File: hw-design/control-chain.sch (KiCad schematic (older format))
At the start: 37 parts, among them J1 RJ45_CHAIN_MAIN, J2 RJ45_CHAIN_EXTENSION, Q1 MMBT3904, Q2 MMBT3906, Q4 MMBT3904, Q5 MMBT3904, Q6 MMBT3904, U4 MAX13450E

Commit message: changing control chain schematic to use default kicad components library
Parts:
- removed J1: RJ45_CHAIN_MAIN, MOD_Footprints_Lib:RJ45-RJHSE5084, symbol RJ45_CHAIN
- removed J2: RJ45_CHAIN_EXTENSION, MOD_Footprints_Lib:RJ45-RJHSE5084, symbol RJ45_CHAIN
- added J? (x2): RJ45_LEDS, symbol RJ45_LEDS
- C18, C20, C6: value 100nF_X7R -> 100nF X7R
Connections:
- net labels added: +3.3VP, GNDD, VDD
- net labels removed: +3.3V, DGND, VCC
- wire segments 133 -> 161
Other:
- moved on the sheet: C19, C20, C5, C6, Q1, Q4, R1, R2, R3, R4, R44, R48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

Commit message: ERC passing
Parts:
- gave numbers to parts that had none: 2
- renumbered C6 to C10, C20 to C11, C18 to C7, C5 to C8, C19 to C9, Q6 to Q1, Q1 to Q2, Q4 to Q3, Q5 to Q4, Q2 to Q5, R54 to R1, R44 to R11, R48 to R12, R31 to R13, R9 to R14, R49 to R15, R52 to R16, R50 to R17, R51 to R18, R12 to R19, R1 to R2, R13 to R20, R53 to R21, R14 to R22, R5 to R3, R6 to R5, R3 to R6, R2 to R8, R8 to R9, U4 to U3
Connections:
- wire segments 161 -> 132

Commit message: wip: footprint association using default kicad libraries
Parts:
- C10, C11, C7: footprint MOD_Footprints_Lib:SM0603 -> Capacitors_SMD:C_0603
- C8, C9: footprint MOD_Footprints_Lib:CAP_RAD_5MM -> Capacitors_ThroughHole:Capacitor5x6RM2.5
- D2, D3: footprint MOD_Footprints_Lib:SOD123 -> Diodes_SMD:SOD-123
- J1, J2: footprint (none) -> MOD_Footprints:RJ45-RJHSE5084
- Q1, Q2, Q3, Q4: footprint (none) -> Transistors_SMD:sot23
- Q5: footprint MOD_Footprints_Lib:SOT23 -> Transistors_SMD:sot23
- R1, R10, R12, R13, R14, R15, R16, R17, R18, R19, R2, R20, R21, R22, R7: footprint MOD_Footprints_Lib:SM0603 -> Resistors_SMD:R_0603
- R11, R3, R4, R5, R6: footprint MOD_Footprints_Lib:SM0805 -> Resistors_SMD:R_0603
- R8, R9: footprint MOD_Footprints_Lib:SM1210 -> Resistors_SMD:R_1210
- U3: footprint TSSOP-14EP -> Housings_SSOP:TSSOP-14_4.4x5mm_Pitch0.65mm
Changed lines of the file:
@@
 F 0 "R5" V 2500 850 40  0000 C CNN
 F 1 "1K2" V 2557 1051 40  0000 C CNN
-F 2 "MOD_Footprints_Lib:SM0805" V 2480 1050 30  0001 C CNN
+F 2 "Resistors_SMD:R_0603" V 2480 1050 30  0001 C CNN
 F 3 "~" H 2550 1050 30  0000 C CNN
 	1    2550 1050
@@
 F 0 "R3" V 2450 1250 40  0000 C CNN
 F 1 "1K2" V 2407 1051 40  0000 C CNN
-F 2 "MOD_Footprints_Lib:SM0805" V 2330 1050 30  0001 C CNN
+F 2 "Resistors_SMD:R_0603" V 2330 1050 30  0001 C CNN
 F 3 "~" H 2400 1050 30  0000 C CNN
 	1    2400 1050
@@
 F 0 "R6" V 2600 4550 40  0000 C CNN
 F 1 "1K2" V 2557 4351 40  0000 C CNN
-F 2 "MOD_Footprints_Lib:SM0805" V 2480 4350 30  0001 C CNN
+F 2 "Resistors_SMD:R_0603" V 2480 4350 30  0001 C CNN
 F 3 "~" H 2550 4350 30  0000 C CNN
 	1    2550 4350
@@
 F 0 "R2" V 1500 2450 40  0000 C CNN
 F 1 "10k" V 1607 2451 40  0000 C CNN
-F 2 "MOD_Footprints_Lib:SM0603" V 1530 2450 30  0001 C CNN
+F 2 "Resistors_SMD:R_0603" V 1530 2450 30  0001 C CNN
 F 3 "~" H 1600 2450 30  0000 C CNN
 	1    1600 2450
@@
 F 0 "R13" V 5050 7050 40  0000 C CNN
 F 1 "10k" V 5007 6801 40  0000 C CNN
-F 2 "MOD_Footprints_Lib:SM0603" V 4930 6800 30  0001 C CNN
+F 2 "Resistors_SMD:R_0603" V 4930 6800 30  0001 C CNN
 F 3 "~" H 5000 6800 30  0000 C CNN
 	1    5000 6800
@@
 F 0 "R7" V 3650 5550 40  0000 C CNN
 F 1 "10k" V 3557 5551 40  0000 C CNN
-F 2 "MOD_Footprints_Lib:SM0603" V 3480 5550 30  0001 C CNN
+F 2 "Resistors_SMD:R_0603" V 3480 5550 30  0001 C CNN
 F 3 "~" H 3550 5550 30  0000 C CNN
 	1    3550 5550
@@
 F 0 "D3" H 1798 6112 40  0000 C CNN
 F 1 "MMSZ5242B" H 1796 5978 30  0000 C CNN
-F 2 "MOD_Footprints_Lib:SOD123" H 1800 6050 60  0001 C CNN
+F 2 "Diodes_SMD:SOD-123" H 1800 6050 60  0001 C CNN
 F 3 "" H 1800 6050 60  0000 C CNN
 	1    1800 6050
@@
 F 0 "D2" H 1598 6112 40  0000 C CNN
 F 1 "MMSZ5242B" H 1598 5984 30  0000 C CNN
-F 2 "MOD_Footprints_Lib:SOD123" H 1600 6050 60  0001 C CNN
+F 2 "Diodes_SMD:SOD-123" H 1600 6050 60  0001 C CNN
 F 3 "" H 1600 6050 60  0000 C CNN
 	1    1600 6050
@@
 F 0 "C7" V 2050 7075 40  0000 L CNN
 F 1 "100nF X7R" V 2125 7075 40  0000 L CNN
-F 2 "MOD_Footprints_Lib:SM0603" H 2038 7100 30  0001 C CNN
+F 2 "Capacitors_SMD:C_0603" H 2038 7100 30  0001 C CNN
 F 3 "~" H 2000 7250 60  0000 C CNN
 	1    2000 7250
@@
 F 0 "R10" V 3900 5550 40  0000 C CNN
 F 1 "10k" V 3807 5551 40  0000 C CNN
-F 2 "MOD_Footprints_Lib:SM0603" V 3730 5550 30  0001 C CNN
+F 2 "Resistors_SMD:R_0603" V 3730 5550 30  0001 C CNN
 F 3 "~" H 3800 5550 30  0000 C CNN
 	1    3800 5550
@@
 F 0 "R11" V 4400 6150 40  0000 C CNN
 F 1 "0R/NC" V 4307 6151 40  0000 C CNN
-F 2 "MOD_Footprints_Lib:SM0805" V 4230 6150 30  0001 C CNN
+F 2 "Resistors_SMD:R_0603" V 4230 6150 30  0001 C CNN
 F 3 "~" H 4300 6150 30  0000 C CNN
 	1    4300 6150
@@
 F 0 "R9" V 3850 4600 40  0000 C CNN
 F 1 "100R 0.5W" V 3700 4350 40  0000 C CNN
-F 2 "MOD_Footprints_Lib:SM1210" V 3730 4350 30  0001 C CNN
+F 2 "Resistors_SMD:R_1210" V 3730 4350 30  0001 C CNN
 F 3 "~" H 3800 4350 30  0000 C CNN
 	1    3800 4350
@@
 F 0 "R8" V 3850 2800 40  0000 C CNN
 F 1 "100R 0.5W" V 3700 2550 40  0000 C CNN
-F 2 "MOD_Footprints_Lib:SM1210" V 3730 2550 30  0001 C CNN
+F 2 "Resistors_SMD:R_1210" V 3730 2550 30  0001 C CNN
 F 3 "~" H 3800 2550 30  0000 C CNN
 	1    3800 2550
@@
 F 0 "C8" V 4550 4350 50  0000 L CNN
 F 1 "100uF" V 4300 4150 50  0000 L CNN
-F 2 "MOD_Footprints_Lib:CAP_RAD_5MM" H 4450 4250 60  0001 C CNN
+F 2 "Capacitors_ThroughHole:Capacitor5x6RM2.5" H 4450 4250 60  0001 C CNN
 F 3 "~" H 4450 4250 60  0000 C CNN
 	1    4450 4250
@@
 F 0 "C10" V 4750 4350 40  0000 L CNN
 F 1 "100nF X7R" V 4950 4100 40  0000 L CNN
-F 2 "MOD_Footprints_Lib:SM0603" H 4838 4100 30  0001 C CNN
+F 2 "Capacitors_SMD:C_0603" H 4838 4100 30  0001 C CNN
 F 3 "~" H 4800 4250 60  0000 C CNN
 	1    4800 4250
@@
 F 0 "R20" V 7350 3000 40  0000 C CNN
 F 1 "10k" V 7457 3001 40  0000 C CNN
-F 2 "MOD_Footprints_Lib:SM0603" V 7380 3000 30  0001 C CNN
+F 2 "Resistors_SMD:R_0603" V 7380 3000 30  0001 C CNN
 F 3 "~" H 7450 3000 30  0000 C CNN
 	1    7450 3000
@@
 F 0 "R19" V 6950 3350 40  0000 C CNN
 F 1 "100k" V 7057 3351 40  0000 C CNN
-F 2 "MOD_Footprints_Lib:SM0603" V 6980 3350 30  0001 C CNN
+F 2 "Resistors_SMD:R_0603" V 6980 3350 30  0001 C CNN
 F 3 "~" H 7050 3350 30  0000 C CNN
 	1    7050 3350
@@
 F 0 "R22" V 8400 4000 40  0000 C CNN
 F 1 "10k" V 8507 4001 40  0000 C CNN
-F 2 "MOD_Footprints_Lib:SM0603" V 8430 4000 30  0001 C CNN
+F 2 "Resistors_SMD:R_0603" V 8430 4000 30  0001 C CNN
 F 3 "~" H 8500 4000 30  0000 C CNN
 	1    8500 4000
@@
 F 0 "Q5" H 8400 3200 50  0000 R CNN
 F 1 "MMBT3906" H 8400 3500 50  0000 R CNN
-F 2 "MOD_Footprints_Lib:SOT23" H 8400 3350 60  0001 C CNN
+F 2 "Transistors_SMD:sot23" H 8400 3350 60  0001 C CNN
 F 3 "" H 8400 3350 60  0000 C CNN
 	1    8400 3350
@@
 F 0 "R12" V 4850 3750 40  0000 C CNN
 F 1 "100k" V 4807 3501 40  0000 C CNN
-F 2 "MOD_Footprints_Lib:SM0603" V 4730 3500 30  0001 C CNN
+F 2 "Resistors_SMD:R_0603" V 4730 3500 30  0001 C CNN
 F 3 "~" H 4800 3500 30  0000 C CNN
 	1    4800 3500
@@
 F 0 "C9" V 4900 2400 50  0000 L CNN
 F 1 "100uF" V 4650 2200 50  0000 L CNN
-F 2 "MOD_Footprints_Lib:CAP_RAD_5MM" H 4800 2300 60  0001 C CNN
+F 2 "Capacitors_ThroughHole:Capacitor5x6RM2.5" H 4800 2300 60  0001 C CNN
 F 3 "~" H 4800 2300 60  0000 C CNN
 	1    4800 2300
@@
 F 0 "C11" V 5100 2400 40  0000 L CNN
 F 1 "100nF X7R" V 5300 2150 40  0000 L CNN
-F 2 "MOD_Footprints_Lib:SM0603" H 5188 2150 30  0001 C CNN
+F 2 "Capacitors_SMD:C_0603" H 5188 2150 30  0001 C CNN
 F 3 "~" H 5150 2300 60  0000 C CNN
 	1    5150 2300
@@
 F 0 "R16" V 5550 2550 40  0000 C CNN
 F 1 "100k" V 5507 2301 40  0000 C CNN
-F 2 "MOD_Footprints_Lib:SM0603" V 5430 2300 30  0001 C CNN
+F 2 "Resistors_SMD:R_0603" V 5430 2300 30  0001 C CNN
 F 3 "~" H 5500 2300 30  0000 C CNN
 	1    5500 2300
@@
 F 0 "R18" V 5900 6350 40  0000 C CNN
 F 1 "10k" V 5857 6101 40  0000 C CNN
-F 2 "MOD_Footprints_Lib:SM0603" V 5780 6100 30  0001 C CNN
+F 2 "Resistors_SMD:R_0603" V 5780 6100 30  0001 C CNN
 F 3 "~" H 5850 6100 30  0000 C CNN
 	1    5850 6100
@@
 F 0 "R17" V 5900 5400 40  0000 C CNN
 F 1 "10k" V 5857 5151 40  0000 C CNN
-F 2 "MOD_Footprints_Lib:SM0603" V 5780 5150 30  0001 C CNN
+F 2 "Resistors_SMD:R_0603" V 5780 5150 30  0001 C CNN
 F 3 "~" H 5850 5150 30  0000 C CNN
 	1    5850 5150
@@
 F 0 "R14" V 5350 5500 40  0000 C CNN
 F 1 "100k" V 5457 5501 40  0000 C CNN
-F 2 "MOD_Footprints_Lib:SM0603" V 5380 5500 30  0001 C CNN
+F 2 "Resistors_SMD:R_0603" V 5380 5500 30  0001 C CNN
 F 3 "~" H 5450 5500 30  0000 C CNN
 	1    5450 5500
@@
 F 0 "R15" V 5350 6450 40  0000 C CNN
 F 1 "100k" V 5457 6451 40  0000 C CNN
-F 2 "MOD_Footprints_Lib:SM0603" V 5380 6450 30  0001 C CNN
+F 2 "Resistors_SMD:R_0603" V 5380 6450 30  0001 C CNN
 F 3 "~" H 5450 6450 30  0000 C CNN
 	1    5450 6450
@@
 F 0 "R21" V 7750 3350 40  0000 C CNN
 F 1 "1k" V 7857 3351 40  0000 C CNN
-F 2 "MOD_Footprints_Lib:SM0603" V 7780 3350 30  0001 C CNN
+F 2 "Resistors_SMD:R_0603" V 7780 3350 30  0001 C CNN
 F 3 "~" H 7850 3350 30  0000 C CNN
 	1    7850 3350
@@
 F 0 "R4" V 2450 4550 40  0000 C CNN
 F 1 "1K2" V 2407 4351 40  0000 C CNN
-F 2 "MOD_Footprints_Lib:SM0805" V 2330 4350 30  0001 C CNN
+F 2 "Resistors_SMD:R_0603" V 2330 4350 30  0001 C CNN
 F 3 "~" H 2400 4350 30  0000 C CNN
 	1    2400 4350
@@
 F 0 "R1" V 1450 3400 40  0000 C CNN
 F 1 "10k" V 1557 3401 40  0000 C CNN
-F 2 "MOD_Footprints_Lib:SM0603" V 1480 3400 30  0001 C CNN
+F 2 "Resistors_SMD:R_0603" V 1480 3400 30  0001 C CNN
 F 3 "~" H 1550 3400 30  0000 C CNN
 	1    1550 3400
@@
 F 0 "U3" H 2700 7100 60  0000 C CNN
 F 1 "MAX13450E" H 2950 5600 60  0000 C CNN
-F 2 "TSSOP-14EP" H 2600 6950 40  0001 C CNN
+F 2 "Housings_SSOP:TSSOP-14_4.4x5mm_Pitch0.65mm" H 2600 6950 40  0001 C CNN
 F 3 "" H 2725 6250 60  0000 C CNN
 	1    2700 6350
@@
 F 0 "Q3" H 5100 5000 50  0000 R CNN
 F 1 "MMBT3904" H 5100 5300 50  0000 R CNN
-F 2 "" H 5100 5150 60  0000 C CNN
+F 2 "Transistors_SMD:sot23" H 5100 5150 60  0001 C CNN
 F 3 "" H 5100 5150 60  0000 C CNN
 	1    5100 5150
@@
 F 0 "Q4" H 5100 5950 50  0000 R CNN
 F 1 "MMBT3904" H 5350 6350 50  0000 R CNN
-F 2 "" H 5100 6100 60  0000 C CNN
+F 2 "Transistors_SMD:sot23" H 5100 6100 60  0001 C CNN
 F 3 "" H 5100 6100 60  0000 C CNN
 	1    5100 6100
@@
 F 0 "Q2" H 2300 2300 50  0000 R CNN
 F 1 "MMBT3904" H 2300 2600 50  0000 R CNN
-F 2 "" H 2300 2450 60  0000 C CNN
+F 2 "Transistors_SMD:sot23" H 2300 2450 60  0001 C CNN
 F 3 "" H 2300 2450 60  0000 C CNN
 	1    2300 2450
@@
 F 0 "Q1" H 2100 3250 50  0000 R CNN
 F 1 "MMBT3904" H 2100 3550 50  0000 R CNN
-F 2 "" H 2100 3400 60  0000 C CNN
+F 2 "Transistors_SMD:sot23" H 2100 3400 60  0001 C CNN
 F 3 "" H 2100 3400 60  0000 C CNN
 	1    2100 3400
@@
 F 0 "J2" H 3200 3050 50  0000 C CNN
 F 1 "RJ45_LEDS" H 3200 3950 50  0000 C CNN
-F 2 "" H 3200 3500 60  0000 C CNN
+F 2 "MOD_Footprints:RJ45-RJHSE5084" H 3200 3500 60  0001 C CNN
 F 3 "" H 3200 3500 60  0000 C CNN
 	1    3200 3550
@@
 F 0 "J1" H 3200 1300 50  0000 C CNN
 F 1 "RJ45_LEDS" H 3200 2200 50  0000 C CNN
-F 2 "" H 3200 1750 60  0000 C CNN
+F 2 "MOD_Footprints:RJ45-RJHSE5084" H 3200 1750 60  0001 C CNN
 F 3 "" H 3200 1750 60  0000 C CNN
 	1    3200 1800

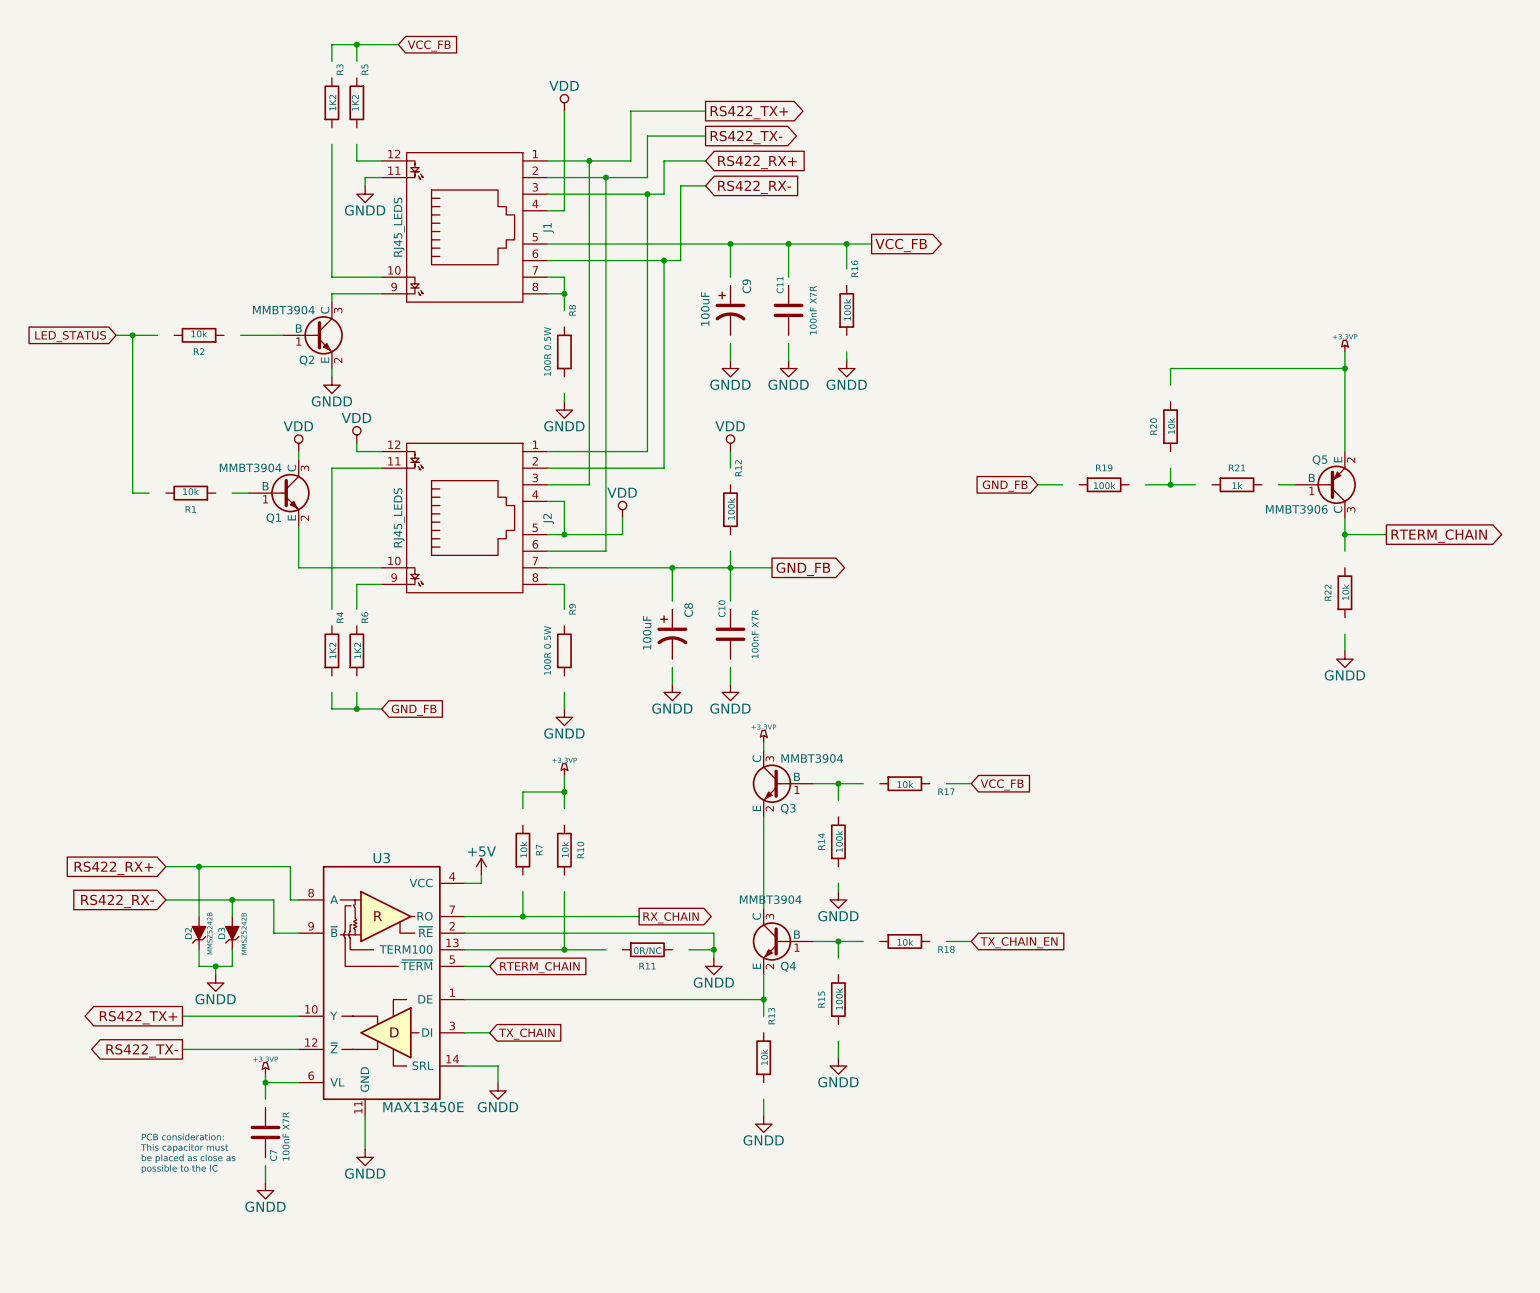
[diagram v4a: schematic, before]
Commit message: adding official kicad library as submodule
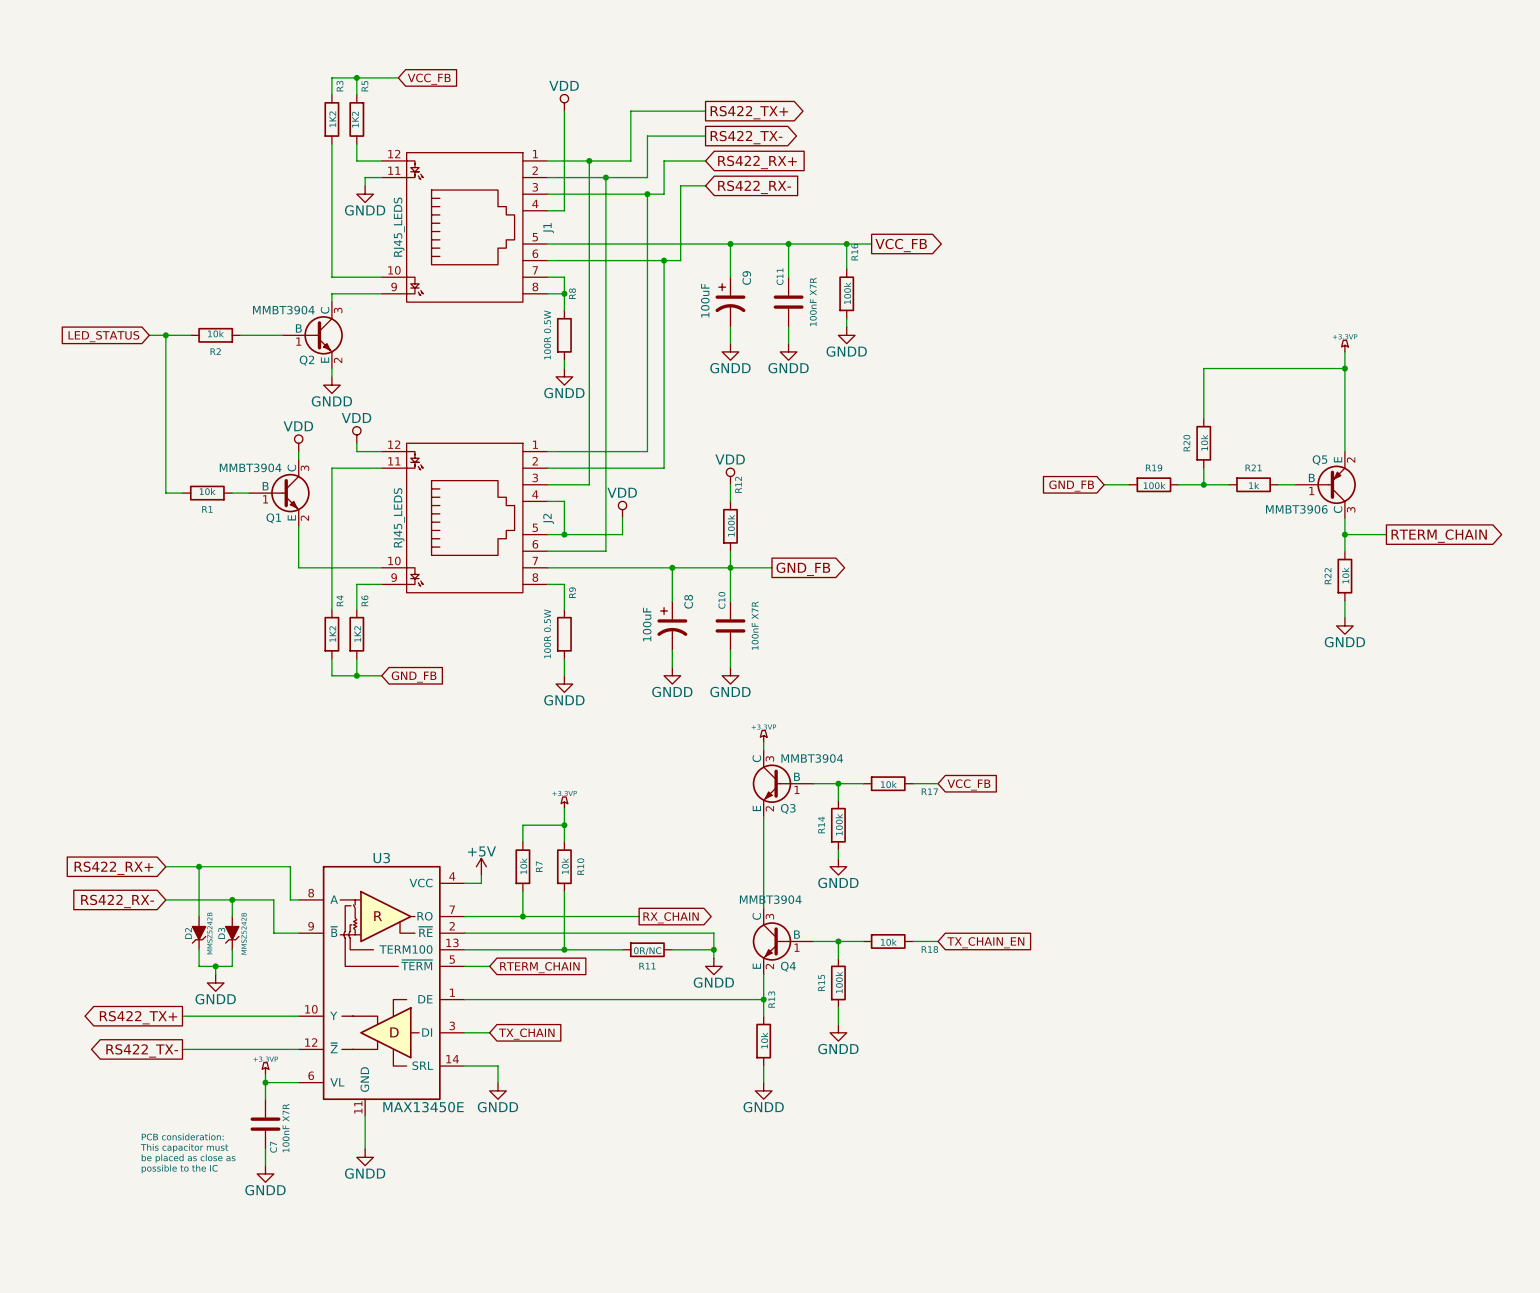
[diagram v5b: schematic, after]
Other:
- moved on the sheet: C10, C11, C7, C8, C9, R1, R10, R12, R13, R14, R15, R16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
